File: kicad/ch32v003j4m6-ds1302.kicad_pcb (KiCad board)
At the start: 2 copper layers, 24.1 x 38.1 mm, 14 parts, among them J1 Conn_01x04_Pin, SW1 SW_Push, U2 DS1302+, Y1 Crystal

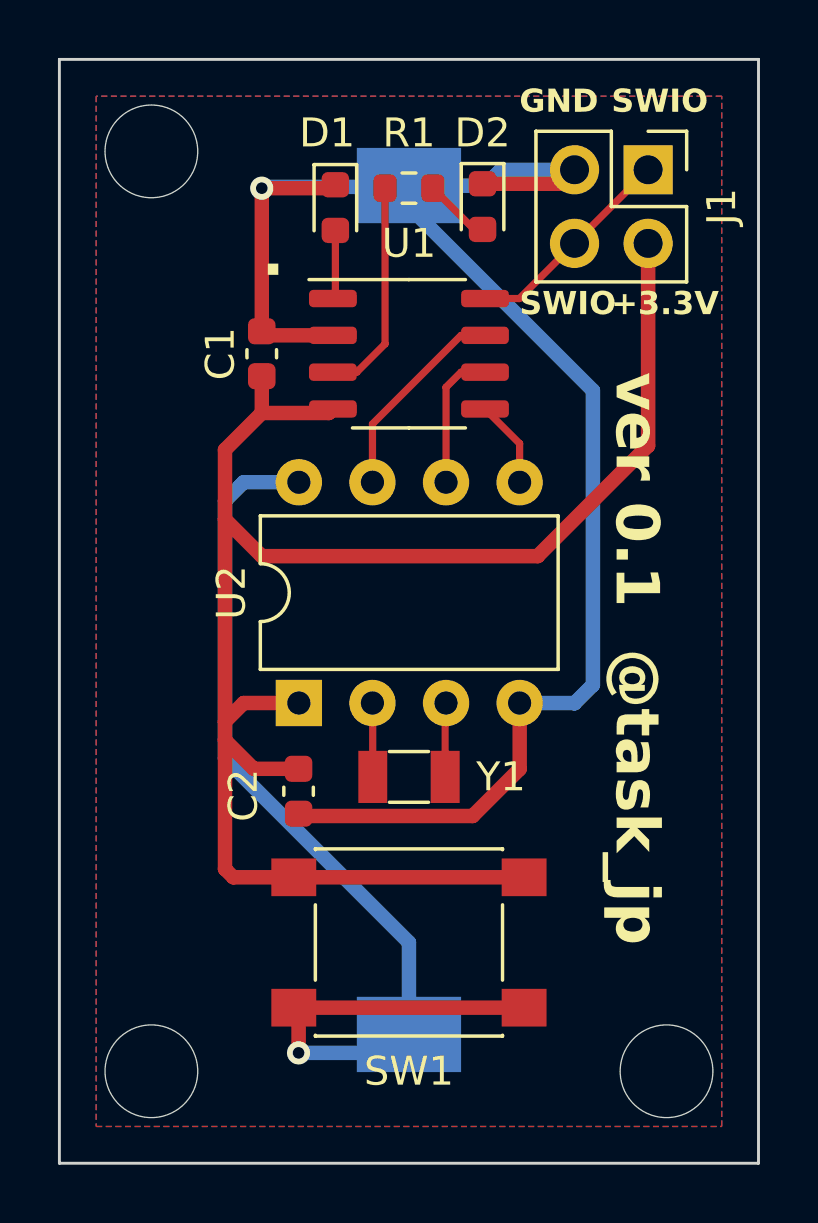
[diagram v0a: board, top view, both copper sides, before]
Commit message: Add a resistor for LED(G)
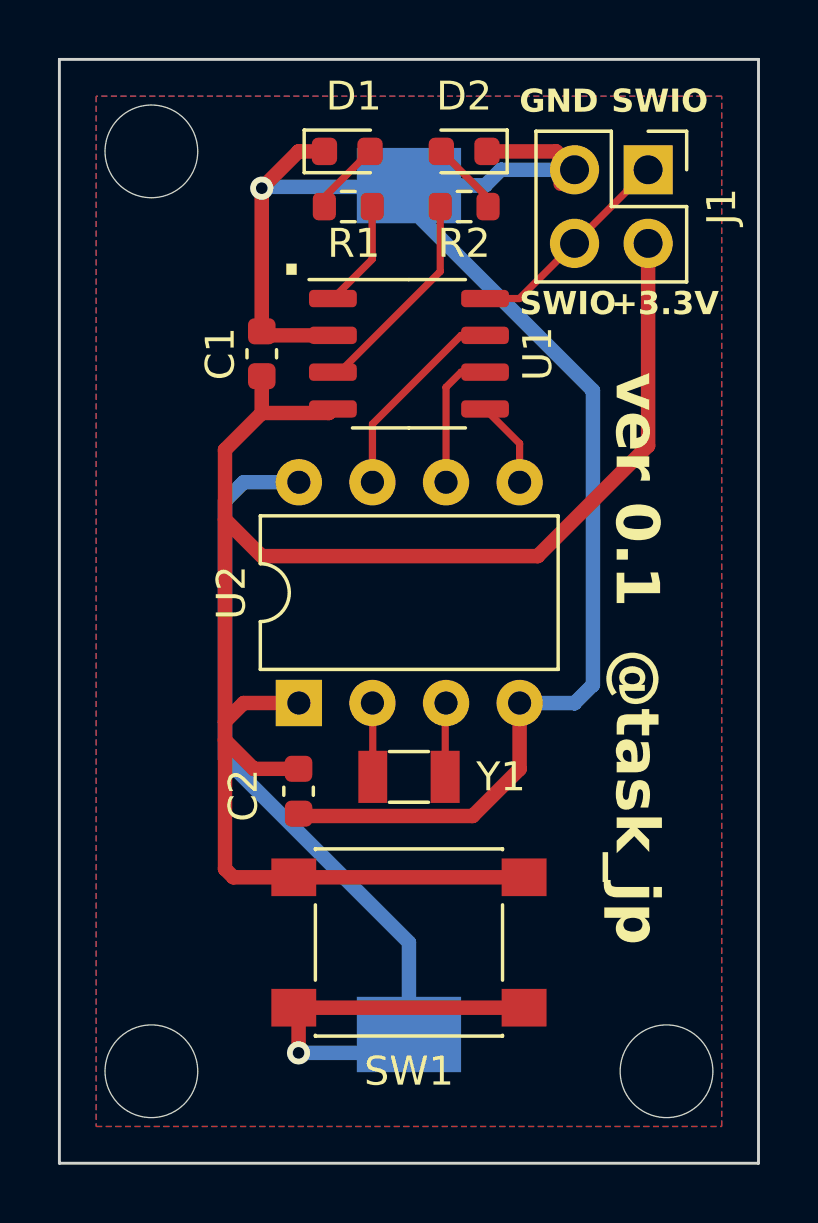
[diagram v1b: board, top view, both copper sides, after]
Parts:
- added R1: R, Resistor_SMD:R_0603_1608Metric, F.Cu at (140.1, 67.3)
- moved R2 2.01 mm to (144.1, 67.3)
- moved D2 2.01 mm to (144.1, 65.4), turned to 180 degrees
- moved D1 1.98 mm to (140.1, 65.4), turned to 0 degrees
- renumbered R1 to R2
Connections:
- U1 pad 1: Net-(D1-A) -> Net-(U1-PA1)
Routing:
- net Net-(U1-PA1): track 0.00 -> 3.74 mm
- net GND: track 58.4 -> 59.1 mm

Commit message: Minimize size
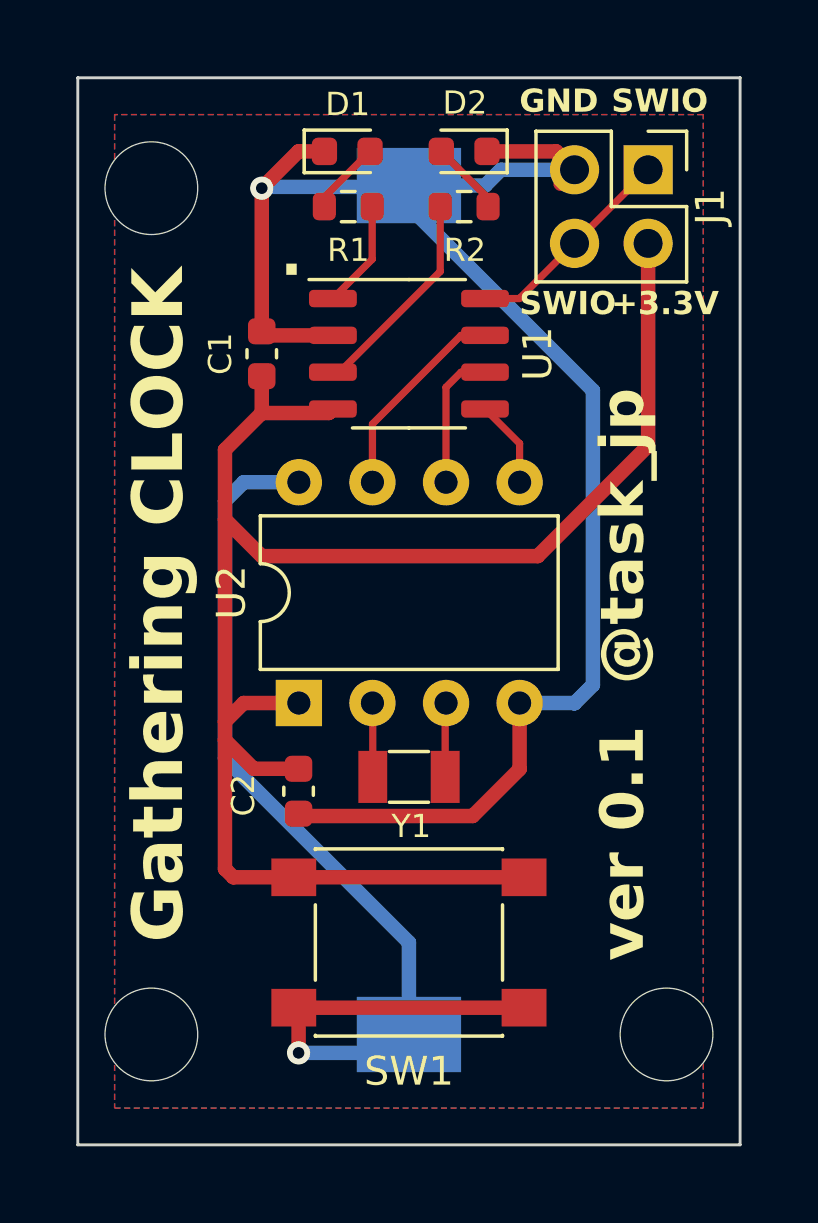
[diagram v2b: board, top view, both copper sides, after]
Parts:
- moved REF** 1.27 mm to (151.1, 95.9)
- moved REF** 1.27 mm to (133.3, 66.7)
- moved REF** 1.27 mm to (133.3, 95.9)
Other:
- board size 24.1 x 38.1 mm -> 22.9 x 36.8 mm
- board text added: "Gathering CLOCK"
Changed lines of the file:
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@@
     (property "ki_keywords" "R res resistor")
     (attr smd)
-    (fp_text reference "R1" (at 0.19 1.27 180) (layer "F.SilkS")
-        (effects (font (size 1 1) (thickness 0.15)))
+    (fp_text reference "R1" (at 0.002199 1.504381 180) (layer "F.SilkS")
+        (effects (font (size 0.8 0.8) (thickness 0.15)))
     )
     (fp_text value "R" (at 0 1.43) (layer "F.Fab")
@@
   )
   (footprint "MountingHole:MountingHole_3.2mm_M3" (layer "F.Cu")
-    (at 151.13 97.155)
+    (at 151.13 95.885)
     (descr "Mounting Hole 3.2mm, no annular, M3")
     (tags "mounting hole 3.2mm no annular m3")
@@
     (property "ki_keywords" "LED diode")
     (attr smd)
-    (fp_text reference "D1" (at 0.225 -1.905 180) (layer "F.SilkS")
-        (effects (font (size 1 1) (thickness 0.15)))
+    (fp_text reference "D1" (at 0.013662 -1.627493 180) (layer "F.SilkS")
+        (effects (font (size 0.8 0.8) (thickness 0.15)))
     )
     (fp_text value "LED(G)" (at 0 1.43) (layer "F.Fab")
@@
     (property "ki_keywords" "R res resistor")
     (attr smd)
-    (fp_text reference "R2" (at 0 -1.27 180) (layer "F.SilkS")
-        (effects (font (size 1 1) (thickness 0.15)))
+    (fp_text reference "R2" (at -0.02403 -1.504381 180) (layer "F.SilkS")
+        (effects (font (size 0.8 0.8) (thickness 0.15)))
     )
     (fp_text value "R" (at 0 1.43) (layer "F.Fab")
@@
     (property "ki_keywords" "connector")
     (attr through_hole)
-    (fp_text reference "J1" (at 2.54 1.27 90) (layer "F.SilkS")
+    (fp_text reference "J1" (at 2.150236 1.268026 90) (layer "F.SilkS")
         (effects (font (size 1 1) (thickness 0.15)))
     )
@@
   )
   (footprint "MountingHole:MountingHole_3.2mm_M3" (layer "F.Cu")
-    (at 133.35 65.405)
+    (at 133.35 66.675)
     (descr "Mounting Hole 3.2mm, no annular, M3")
     (tags "mounting hole 3.2mm no annular m3")
@@
     (attr smd)
     (fp_text reference "C1" (at 0 -1.43 90) (layer "F.SilkS")
-        (effects (font (size 1 1) (thickness 0.15)))
+        (effects (font (size 0.8 0.8) (thickness 0.15)))
     )
     (fp_text value "C" (at 0 1.43 90) (layer "F.Fab")
@@
   )
   (footprint "MountingHole:MountingHole_3.2mm_M3" (layer "F.Cu")
-    (at 133.35 97.155)
+    (at 133.35 95.885)
     (descr "Mounting Hole 3.2mm, no annular, M3")
     (tags "mounting hole 3.2mm no annular m3")
@@
     (property "ki_keywords" "quartz ceramic resonator oscillator")
     (attr smd)
-    (fp_text reference "Y1" (at 3.175 0) (layer "F.SilkS")
-        (effects (font (size 1 1) (thickness 0.15)))
+    (fp_text reference "Y1" (at 0.07848 1.704024) (layer "F.SilkS")
+        (effects (font (size 0.8 0.8) (thickness 0.15)))
     )
     (fp_text value "Crystal" (at 0 2) (layer "F.Fab")
@@
     (property "ki_keywords" "LED diode")
     (attr smd)
-    (fp_text reference "D2" (at 0 1.905 180) (layer "F.SilkS")
-        (effects (font (size 1 1) (thickness 0.15)))
+    (fp_text reference "D2" (at -0.02699 1.674567 180) (layer "F.SilkS")
+        (effects (font (size 0.8 0.8) (thickness 0.15)))
     )
     (fp_text value "LED(R)" (at 0 1.43) (layer "F.Fab")
@@
     (attr smd)
     (fp_text reference "C2" (at 0.14 1.905 90) (layer "F.SilkS")
-        (effects (font (size 1 1) (thickness 0.15)))
+        (effects (font (size 0.8 0.8) (thickness 0.15)))
     )
     (fp_text value "C" (at 0 1.43 90) (layer "F.Fab")
@@
     )
   )
-  (gr_rect (start 130.175 62.23) (end 154.305 100.33)
+  (gr_rect (start 130.81 62.865) (end 153.67 99.695)
     (stroke (width 0.1) (type default)) (fill none) (layer "Edge.Cuts"))
-  (gr_text "ver 0.1  @task_jp" (at 149.225 73.025 270) (layer "F.SilkS")
+  (gr_text "ver 0.1  @task_jp" (at 150.495 93.345 90) (layer "F.SilkS")
     (effects (font (size 1.5 1.5) (thickness 0.3) bold) (justify left bottom))
   )
@@
   (gr_text "." (at 137.795 69.85) (layer "F.SilkS")
     (effects (font (size 1.5 1.5) (thickness 0.3) bold) (justify left bottom))
+  )
+  (gr_text "Gathering CLOCK" (at 134.62 92.71 90) (layer "F.SilkS")
+    (effects (font (size 1.75 1.75) (thickness 0.35) bold) (justify left bottom))
   )
   (gr_text "SWIO" (at 146.05 71.12) (layer "F.SilkS")
@@
     (polygon
       (pts
-        (xy 153.035 63.5)
-        (xy 131.445 63.5)
-        (xy 131.445 99.06)
-        (xy 153.035 99.06)
+        (xy 152.4 64.135)
+        (xy 132.08 64.135)
+        (xy 132.08 98.425)
+        (xy 152.4 98.425)
       )
     )
@@
     (polygon
       (pts
-        (xy 153.035 63.5)
-        (xy 131.445 63.5)
-        (xy 131.445 99.06)
-        (xy 153.035 99.06)
+        (xy 152.4 64.135)
+        (xy 132.08 64.135)
+        (xy 132.08 98.425)
+        (xy 152.4 98.425)
       )
     )

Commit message: Fix mouting hole
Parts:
- removed REF** (x3): MountingHole_3.2mm_M3, MountingHole:MountingHole_3.2mm_M3
- added H1: MountingHole, MountingHole:MountingHole_3.2mm_M3, F.Cu at (133.3, 66.7)
- added H2: MountingHole, MountingHole:MountingHole_3.2mm_M3, F.Cu at (133.3, 95.8)
- added H3: MountingHole, MountingHole:MountingHole_3.2mm_M3, F.Cu at (151.1, 95.8)
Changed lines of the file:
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@@
     )
-  )
-  (footprint "MountingHole:MountingHole_3.2mm_M3" (layer "F.Cu")
-    (at 151.13 95.885)
-    (descr "Mounting Hole 3.2mm, no annular, M3")
-    (tags "mounting hole 3.2mm no annular m3")
-    (attr exclude_from_pos_files exclude_from_bom)
-    (fp_text reference "REF**" (at 0 -4.2) (layer "F.SilkS") hide
-        (effects (font (size 1 1) (thickness 0.15)))
-    )
-    (fp_text value "MountingHole_3.2mm_M3" (at 0 4.2) (layer "F.Fab")
-        (effects (font (size 1 1) (thickness 0.15)))
-    )
-    (fp_text user "${REFERENCE}" (at 0 0) (layer "F.Fab")
-        (effects (font (size 1 1) (thickness 0.15)))
-    )
-    (fp_circle (center 0 0) (end 3.2 0)
-      (stroke (width 0.15) (type solid)) (fill none) (layer "Cmts.User"))
-    (fp_circle (center 0 0) (end 3.45 0)
-      (stroke (width 0.05) (type solid)) (fill none) (layer "F.CrtYd"))
-    (pad "" np_thru_hole circle (at 0 0) (size 3.2 3.2) (drill 3.2) (layers "*.Cu" "*.Mask"))
   )
   (footprint "LED_SMD:LED_0603_1608Metric" (layer "F.Cu")
@@
   )
   (footprint "MountingHole:MountingHole_3.2mm_M3" (layer "F.Cu")
-    (at 133.35 66.675)
+    (at 133.35 95.758)
     (descr "Mounting Hole 3.2mm, no annular, M3")
     (tags "mounting hole 3.2mm no annular m3")
-    (attr exclude_from_pos_files exclude_from_bom)
-    (fp_text reference "REF**" (at 0 -4.2) (layer "F.SilkS") hide
-        (effects (font (size 1 1) (thickness 0.15)))
-    )
-    (fp_text value "MountingHole_3.2mm_M3" (at 0 4.2) (layer "F.Fab")
+    (property "Sheetfile" "ch32v003j4m6-ds1302.kicad_sch")
+    (property "Sheetname" "")
+    (property "ki_description" "Mounting Hole without connection")
+    (property "ki_keywords" "mounting hole")
+    (attr exclude_from_pos_files)
+    (fp_text reference "H2" (at 2.794 -0.254 90) (layer "F.SilkS")
+        (effects (font (size 1 1) (thickness 0.15)))
+    )
+    (fp_text value "MountingHole" (at 0 4.2) (layer "F.Fab")
         (effects (font (size 1 1) (thickness 0.15)))
     )
@@
   )
   (footprint "MountingHole:MountingHole_3.2mm_M3" (layer "F.Cu")
-    (at 133.35 95.885)
+    (at 151.13 95.758)
     (descr "Mounting Hole 3.2mm, no annular, M3")
     (tags "mounting hole 3.2mm no annular m3")
-    (attr exclude_from_pos_files exclude_from_bom)
-    (fp_text reference "REF**" (at 0 -4.2) (layer "F.SilkS") hide
-        (effects (font (size 1 1) (thickness 0.15)))
-    )
-    (fp_text value "MountingHole_3.2mm_M3" (at 0 4.2) (layer "F.Fab")
+    (property "Sheetfile" "ch32v003j4m6-ds1302.kicad_sch")
+    (property "Sheetname" "")
+    (property "ki_description" "Mounting Hole without connection")
+    (property "ki_keywords" "mounting hole")
+    (attr exclude_from_pos_files)
+    (fp_text reference "H3" (at -2.794 0 90) (layer "F.SilkS")
+        (effects (font (size 1 1) (thickness 0.15)))
+    )
+    (fp_text value "MountingHole" (at 0 4.2) (layer "F.Fab")
         (effects (font (size 1 1) (thickness 0.15)))
     )
@@
     )
   )
+  (footprint "MountingHole:MountingHole_3.2mm_M3" (layer "F.Cu")
+    (at 133.35 66.65)
+    (descr "Mounting Hole 3.2mm, no annular, M3")
+    (tags "mounting hole 3.2mm no annular m3")
+    (property "Sheetfile" "ch32v003j4m6-ds1302.kicad_sch")
+    (property "Sheetname" "")
+    (property "ki_description" "Mounting Hole without connection")
+    (property "ki_keywords" "mounting hole")
+    (attr exclude_from_pos_files)
+    (fp_text reference "H1" (at 2.54 0.152 90) (layer "F.SilkS")
+        (effects (font (size 1 1) (thickness 0.15)))
+    )
+    (fp_text value "MountingHole" (at 0 4.2) (layer "F.Fab")
+        (effects (font (size 1 1) (thickness 0.15)))
+    )
+    (fp_text user "${REFERENCE}" (at 0 0) (layer "F.Fab")
+        (effects (font (size 1 1) (thickness 0.15)))
+    )
+    (fp_circle (center 0 0) (end 3.2 0)
+      (stroke (width 0.15) (type solid)) (fill none) (layer "Cmts.User"))
+    (fp_circle (center 0 0) (end 3.45 0)
+      (stroke (width 0.05) (type solid)) (fill none) (layer "F.CrtYd"))
+    (pad "" np_thru_hole circle (at 0 0) (size 3.2 3.2) (drill 3.2) (layers "*.Cu" "*.Mask"))
+  )
   (footprint "LED_SMD:LED_0603_1608Metric" (layer "F.Cu")
